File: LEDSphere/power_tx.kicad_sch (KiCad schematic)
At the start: 87 parts, among them J1 USB_C_Receptacle_USB2.0, M1 Motor_DC, Q1 BSS138, Q2 BSS138, Q3 BSS138, Q4 BSS138, Q5 BSS138, Q6 BSS138, Q7 Si2319CDS, Q8 Si2319CDS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

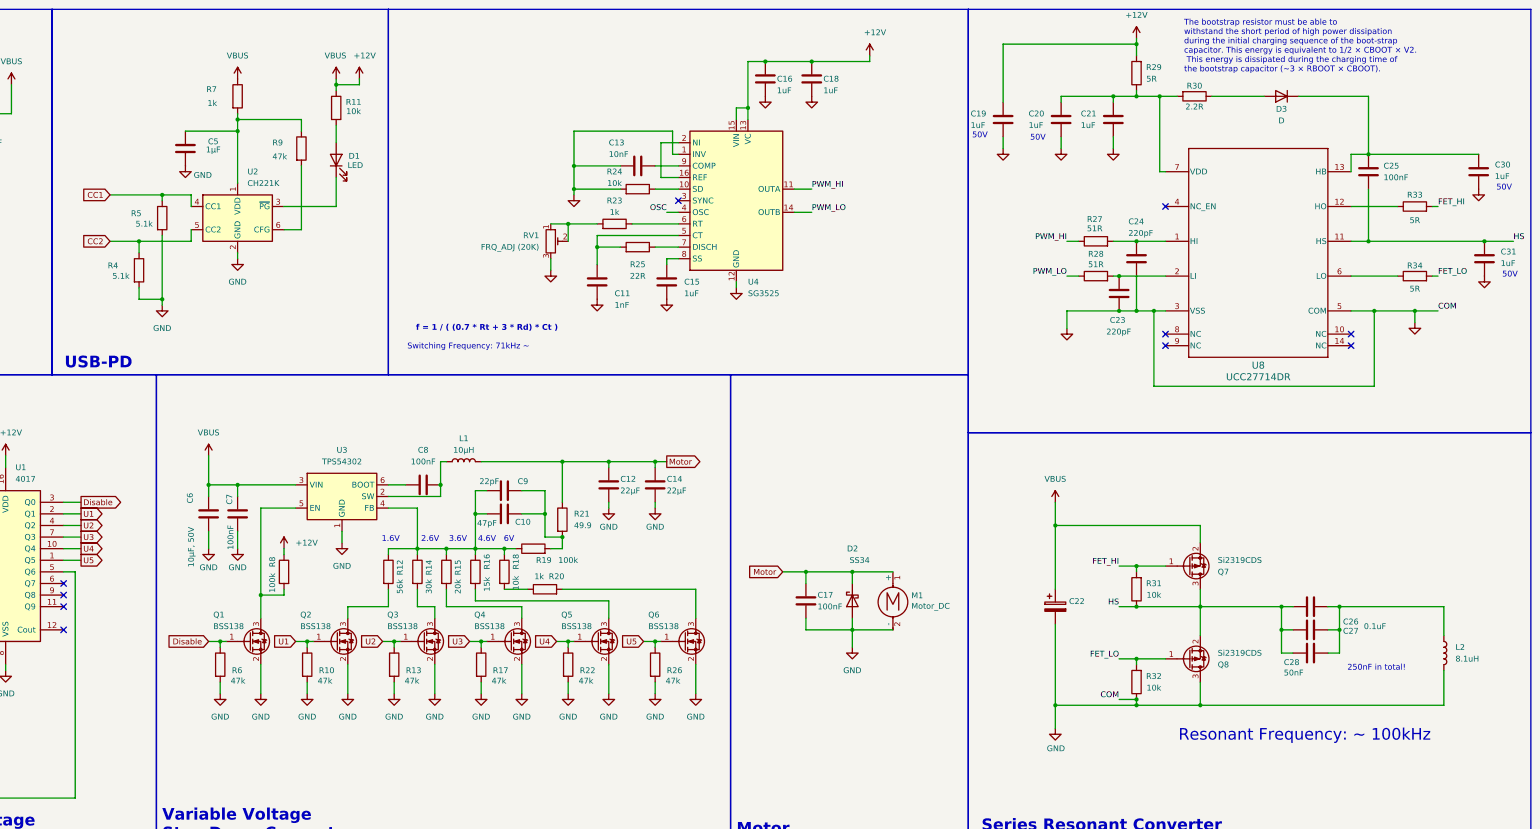
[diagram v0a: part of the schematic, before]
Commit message: Excluded Ground Pour
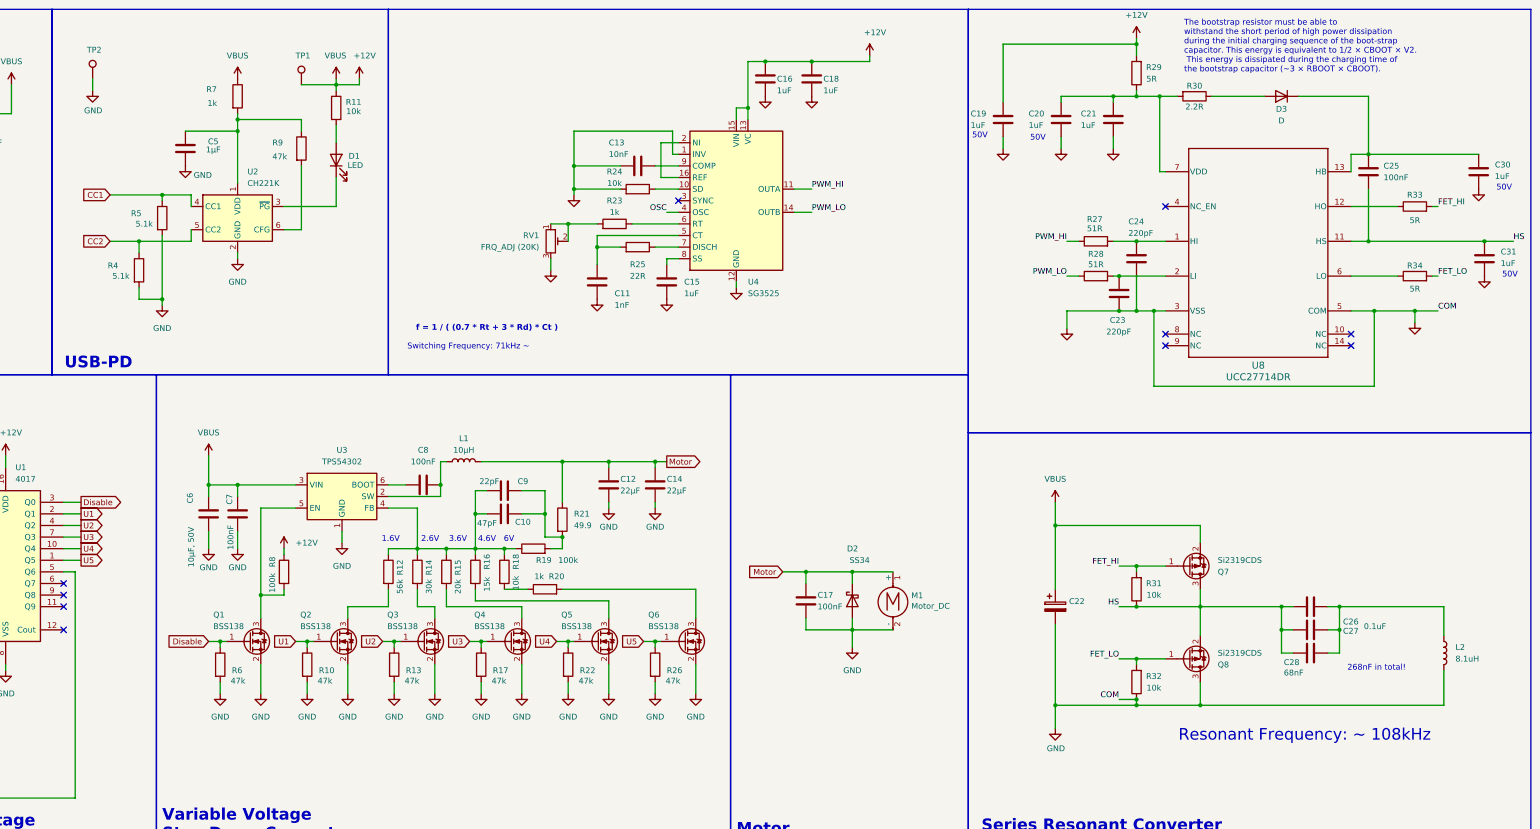
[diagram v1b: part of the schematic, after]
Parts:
- added TP1: TestPoint, TestPoint:TestPoint_Loop_D1.80mm_Drill1.0mm_Beaded, symbol Connector:TestPoint
- added TP2: TestPoint, TestPoint:TestPoint_Pad_D1.0mm, symbol Connector:TestPoint
- C28: value 50nF -> 68nF
- U8: footprint Footprints:D0014A -> Footprints:SOIC127P600X175-14N
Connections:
- net +12V: now also TP1.1
- net GND: now also TP2.1
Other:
- note added: "268nF in total!"
- note added: "Resonant Frequency: ~ 108kHz"
- note removed: "250nF in total!"
- note removed: "Resonant Frequency: ~ 100kHz"

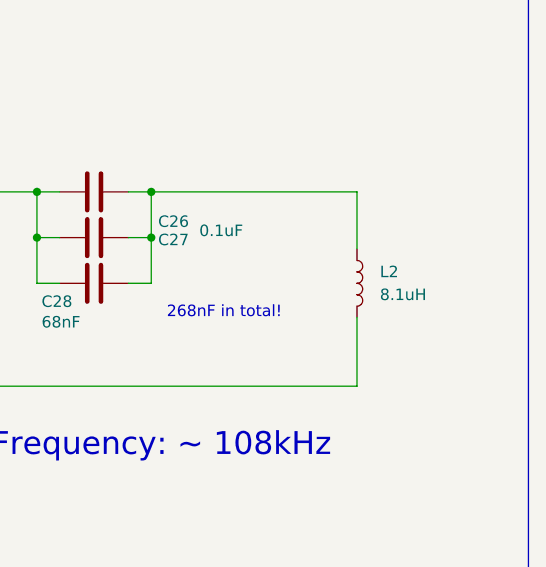
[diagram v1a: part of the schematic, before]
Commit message: Modify RX Schm. + Adjusted TX Coil
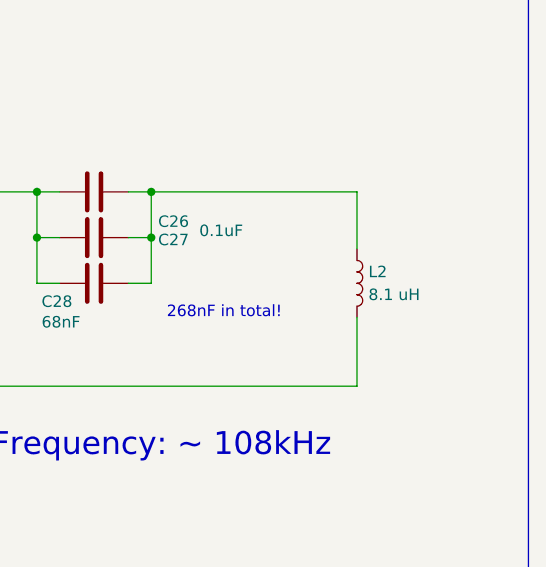
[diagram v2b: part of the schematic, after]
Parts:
- L2: value 8.1uH -> 8.1 uH
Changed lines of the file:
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@@
-	)
-	(symbol
-		(lib_id "Device:L")
-		(at 388.62 153.67 0)
-		(unit 1)
-		(body_style 1)
-		(exclude_from_sim no)
-		(in_bom yes)
-		(on_board yes)
-		(in_pos_files yes)
-		(dnp no)
-		(property "Reference" "L2"
-			(at 391.16 152.3999 0)
-			(show_name no)
-			(do_not_autoplace no)
-			(effects
-				(font
-					(size 1.27 1.27)
-				)
-				(justify left)
-			)
-		)
-		(property "Value" "8.1uH"
-			(at 391.16 154.94 0)
-			(show_name no)
-			(do_not_autoplace no)
-			(effects
-				(font
-					(size 1.27 1.27)
-				)
-				(justify left)
-			)
-		)
-		(property "Footprint" "Footprints:power_coil"
-			(at 388.62 153.67 0)
-			(hide yes)
-			(show_name no)
-			(do_not_autoplace no)
-			(effects
-				(font
-					(size 1.27 1.27)
-				)
-			)
-		)
-		(property "Datasheet" ""
-			(at 388.62 153.67 0)
-			(hide yes)
-			(show_name no)
-			(do_not_autoplace no)
-			(effects
-				(font
-					(size 1.27 1.27)
-				)
-			)
-		)
-		(property "Description" "Inductor"
-			(at 388.62 153.67 0)
-			(hide yes)
-			(show_name no)
-			(do_not_autoplace no)
-			(effects
-				(font
-					(size 1.27 1.27)
-				)
-			)
-		)
-		(pin "2"
-		)
-		(pin "1"
-		)
-		(instances
-			(project "power_tx"
-				(path "/f4cb5b8b-e797-4af7-88e9-03d9cedfe909"
-					(reference "L2")
-					(unit 1)
-				)
-			)
-		)
 	)
 	(symbol
@@
 					(unit 1)
 				)
+			)
+		)
+	)
+	(symbol
+		(lib_id "Device:L")
+		(at 388.62 153.67 0)
+		(unit 1)
+		(body_style 1)
+		(exclude_from_sim no)
+		(in_bom yes)
+		(on_board yes)
+		(in_pos_files yes)
+		(dnp no)
+		(fields_autoplaced yes)
+		(property "Reference" "L2"
+			(at 389.89 152.3999 0)
+			(show_name no)
+			(do_not_autoplace no)
+			(effects
+				(font
+					(size 1.27 1.27)
+				)
+				(justify left)
+			)
+		)
+		(property "Value" "8.1 uH"
+			(at 389.89 154.9399 0)
+			(show_name no)
+			(do_not_autoplace no)
+			(effects
+				(font
+					(size 1.27 1.27)
+				)
+				(justify left)
+			)
+		)
+		(property "Footprint" "Footprints:power_coil"
+			(at 388.62 153.67 0)
+			(hide yes)
+			(show_name no)
+			(do_not_autoplace no)
+			(effects
+				(font
+					(size 1.27 1.27)
+				)
+			)
+		)
+		(property "Datasheet" ""
+			(at 388.62 153.67 0)
+			(hide yes)
+			(show_name no)
+			(do_not_autoplace no)
+			(effects
+				(font
+					(size 1.27 1.27)
+				)
+			)
+		)
+		(property "Description" "Inductor"
+			(at 388.62 153.67 0)
+			(hide yes)
+			(show_name no)
+			(do_not_autoplace no)
+			(effects
+				(font
+					(size 1.27 1.27)
+				)
+			)
+		)
+		(pin "1"
+		)
+		(pin "2"
+		)
+		(instances
+			(project "power_tx"
+				(path "/f4cb5b8b-e797-4af7-88e9-03d9cedfe909"
+					(reference "L2")
+					(unit 1)
+				)

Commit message: Most Recent TX Board Changes
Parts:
- added C29: 68nF, Capacitor_SMD:C_0603_1608Metric, symbol Device:C
- added TP3: TestPoint, TestPoint:TestPoint_Loop_D1.80mm_Drill1.0mm_Beaded, symbol Connector:TestPoint
- L2: value 8.1 uH -> 5.8 uH
- TP2: footprint TestPoint:TestPoint_Pad_D1.0mm -> TestPoint:TestPoint_Loop_D1.80mm_Drill1.0mm_Beaded
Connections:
- net HS: now also C29.1
- net OSC: now also TP3.1
- net at C26.2, C27.2, C28.2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: now also C29.2
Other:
- note added: "400nF in total!"
- note added: "Resonant Frequency: ~ 104kHz"
- note removed: "268nF in total!"
- note removed: "Resonant Frequency: ~ 108kHz"

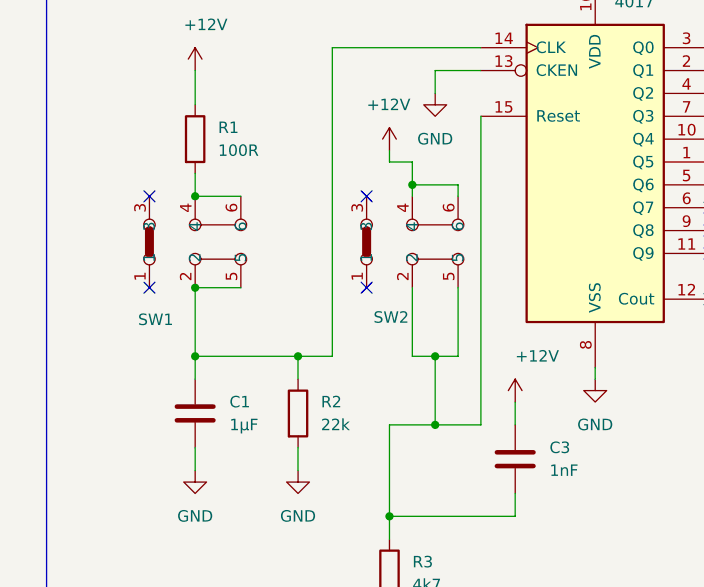
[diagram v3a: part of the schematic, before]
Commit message: Altered Button Part
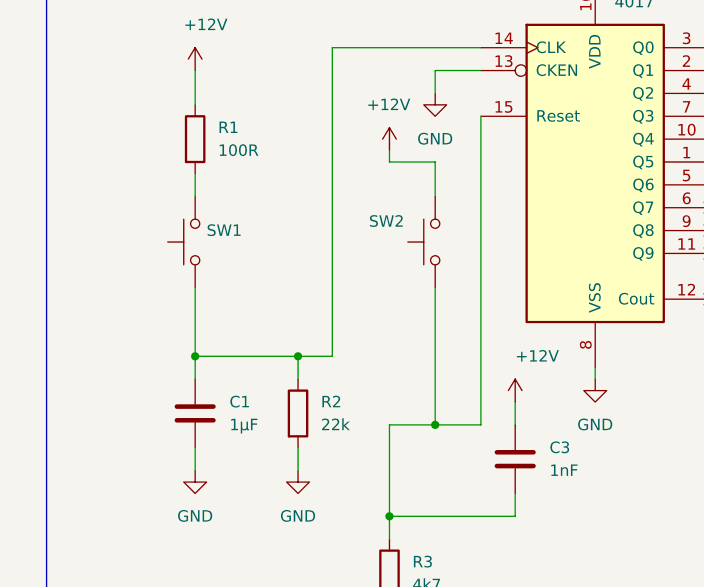
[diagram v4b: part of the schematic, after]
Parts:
- removed SW1, SW2: (no value), Footprints:XKB5858-X-F-75, symbol New_Library:XKB5858-X-F-75
- added SW1, SW2: SW_Push, Button_Switch_THT:SW_Tactile_SPST_Angled_PTS645Vx58-2LFS, symbol Switch:SW_Push
- D2: footprint Footprints:DIOM7959X262N -> Diode_SMD:D_SMA
- L1: footprint Inductor_SMD:L_Bourns_SRP7028A_7.3x6.6mm -> Inductor_SMD:L_Vishay_IHLP-3232; LCSC C5189958 -> (none)
- Q1: LCSC C7420339 -> (none)
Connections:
- net +12V: now also SW2.2
- net at C3.2, R3.1, U1.15 (Reset): now also SW2.1
- net at R1.2: now also SW1.2
- net at C1.1, R2.1, U1.14 (CLK): now also SW1.1
- no-connect marks 17 -> 13

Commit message: Edit 22uF Footprint to 1210
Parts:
- C12, C14: footprint Capacitor_SMD:C_0805_2012Metric -> Capacitor_SMD:C_1210_3225Metric
- D1: LCSC C84256 -> LSM0805412V
- SW1, SW2: Part # (none) -> PTS645VK58-2 LFS
- U1: LCSC C22390236 -> (none); Part # (none) -> CD4017BM96
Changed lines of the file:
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@@
 			)
 		)
-		(property "LCSC" "C84256"
+		(property "LCSC" "LSM0805412V"
 			(at 146.05 45.72 0)
 			(hide yes)
@@
 			)
 		)
-		(property "Datasheet" ""
+		(property "Datasheet" "https://www.digikey.com/en/products/detail/c-k/PTS645VK58-2-LFS/3861398"
 			(at 50.8 142.24 0)
 			(hide yes)
@@
 			)
 		)
+		(property "Part #" "PTS645VK58-2 LFS"
+			(at 55.88 142.24 90)
+			(hide yes)
+			(show_name no)
+			(do_not_autoplace no)
+			(effects
+				(font
+					(size 1.27 1.27)
+				)
+			)
+		)
 		(pin "1"
 		)
@@
 			)
 		)
-		(property "Description" "Trim-potentiometer"
+		(property "Description" "3362P-1-203LF"
 			(at 193.04 63.5 0)
 			(hide yes)
@@
 			)
 		)
-		(property "Datasheet" ""
+		(property "Datasheet" "https://www.digikey.com/en/products/detail/c-k/PTS645VK58-2-LFS/3861398"
 			(at 24.13 142.24 0)
 			(hide yes)
@@
 			)
 		)
+		(property "Part #" "PTS645VK58-2 LFS"
+			(at 29.21 142.24 90)
+			(hide yes)
+			(show_name no)
+			(do_not_autoplace no)
+			(effects
+				(font
+					(size 1.27 1.27)
+				)
+			)
+		)
 		(pin "1"
 		)
@@
 			)
 		)
-		(property "Footprint" "Capacitor_SMD:C_0805_2012Metric"
+		(property "Footprint" "Capacitor_SMD:C_1210_3225Metric"
 			(at 216.8652 120.65 0)
 			(hide yes)
@@
 			)
 		)
-		(property "LCSC" "C22390236"
+		(property "Part #" "CD4017BM96"
 			(at 73.66 133.35 0)
 			(hide yes)
@@
 			)
 		)
-		(property "Footprint" "Capacitor_SMD:C_0805_2012Metric"
+		(property "Footprint" "Capacitor_SMD:C_1210_3225Metric"
 			(at 206.7052 120.65 0)
 			(hide yes)

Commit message: Most up to date TX
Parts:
- added TP4, TP5: TestPoint, TestPoint:TestPoint_Pad_1.0x1.0mm, symbol Connector:TestPoint
- TP1, TP2, TP3: footprint TestPoint:TestPoint_Loop_D1.80mm_Drill1.0mm_Beaded -> TestPoint:TestPoint_THTPad_D2.0mm_Drill1.0mm
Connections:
- net GND: now also TP5.1
- net at C26.2, C27.2, C28.2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: now also TP4.1
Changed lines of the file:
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@@
 	)
 	(junction
+		(at 388.62 143.51)
+		(diameter 0)
+		(color 0 0 0 0)
+	)
+	(junction
 		(at 321.31 20.32)
 		(diameter 0)
@@
 	)
 	(junction
+		(at 388.62 165.1)
+		(diameter 0)
+		(color 0 0 0 0)
+	)
+	(junction
 		(at 120.65 151.13)
 		(diameter 0)
@@
 	(wire
 		(pts
+			(xy 388.62 165.1) (xy 394.97 165.1)
+		)
+		(stroke
+			(width 0)
+			(type default)
+		)
+	)
+	(wire
+		(pts
 			(xy 134.62 139.7) (xy 134.62 140.97)
 		)
@@
 	(wire
 		(pts
+			(xy 388.62 143.51) (xy 393.7 143.51)
+		)
+		(stroke
+			(width 0)
+			(type default)
+		)
+	)
+	(wire
+		(pts
 			(xy 167.64 143.51) (xy 167.64 146.05)
 		)
@@
 			)
 		)
-		(property "Footprint" "TestPoint:TestPoint_Loop_D1.80mm_Drill1.0mm_Beaded"
+		(property "Footprint" "TestPoint:TestPoint_THTPad_D2.0mm_Drill1.0mm"
 			(at 97.79 27.94 0)
 			(hide yes)
@@
 	)
 	(symbol
+		(lib_id "Connector:TestPoint")
+		(at 394.97 165.1 0)
+		(unit 1)
+		(body_style 1)
+		(exclude_from_sim no)
+		(in_bom yes)
+		(on_board yes)
+		(in_pos_files yes)
+		(dnp no)
+		(fields_autoplaced yes)
+		(property "Reference" "TP5"
+			(at 397.51 160.5279 0)
+			(show_name no)
+			(do_not_autoplace no)
+			(effects
+				(font
+					(size 1.27 1.27)
+				)
+				(justify left)
+			)
+		)
+		(property "Value" "TestPoint"
+			(at 397.51 163.0679 0)
+			(show_name no)
+			(do_not_autoplace no)
+			(effects
+				(font
+					(size 1.27 1.27)
+				)
+				(justify left)
+			)
+		)
+		(property "Footprint" "TestPoint:TestPoint_Pad_1.0x1.0mm"
+			(at 400.05 165.1 0)
+			(hide yes)
+			(show_name no)
+			(do_not_autoplace no)
+			(effects
+				(font
+					(size 1.27 1.27)
+				)
+			)
+		)
+		(property "Datasheet" ""
+			(at 400.05 165.1 0)
+			(hide yes)
+			(show_name no)
+			(do_not_autoplace no)
+			(effects
+				(font
+					(size 1.27 1.27)
+				)
+			)
+		)
+		(property "Description" "test point"
+			(at 394.97 165.1 0)
+			(hide yes)
+			(show_name no)
+			(do_not_autoplace no)
+			(effects
+				(font
+					(size 1.27 1.27)
+				)
+			)
+		)
+		(pin "1"
+		)
+		(instances
+			(project "power_tx"
+				(path "/f4cb5b8b-e797-4af7-88e9-03d9cedfe909"
+					(reference "TP5")
+					(unit 1)
+				)
+			)
+		)
+	)
+	(symbol
 		(lib_id "Device:R")
 		(at 382.27 55.88 90)
@@
 			)
 		)
-		(property "Footprint" "TestPoint:TestPoint_Loop_D1.80mm_Drill1.0mm_Beaded"
+		(property "Footprint" "TestPoint:TestPoint_THTPad_D2.0mm_Drill1.0mm"
 			(at 143.51 29.21 0)
 			(hide yes)
@@
 	)
 	(symbol
+		(lib_id "Connector:TestPoint")
+		(at 393.7 143.51 0)
+		(unit 1)
+		(body_style 1)
+		(exclude_from_sim no)
+		(in_bom yes)
+		(on_board yes)
+		(in_pos_files yes)
+		(dnp no)
+		(fields_autoplaced yes)
+		(property "Reference" "TP4"
+			(at 396.24 138.9379 0)
+			(show_name no)
+			(do_not_autoplace no)
+			(effects
+				(font
+					(size 1.27 1.27)
+				)
+				(justify left)
+			)
+		)
+		(property "Value" "TestPoint"
+			(at 396.24 141.4779 0)
+			(show_name no)
+			(do_not_autoplace no)
+			(effects
+				(font
+					(size 1.27 1.27)
+				)
+				(justify left)
+			)
+		)
+		(property "Footprint" "TestPoint:TestPoint_Pad_1.0x1.0mm"
+			(at 398.78 143.51 0)
+			(hide yes)
+			(show_name no)
+			(do_not_autoplace no)
+			(effects
+				(font
+					(size 1.27 1.27)
+				)
+			)
+		)
+		(property "Datasheet" ""
+			(at 398.78 143.51 0)
+			(hide yes)
+			(show_name no)
+			(do_not_autoplace no)
+			(effects
+				(font
+					(size 1.27 1.27)
+				)
+			)
+		)
+		(property "Description" "test point"
+			(at 393.7 143.51 0)
+			(hide yes)
+			(show_name no)
+			(do_not_autoplace no)
+			(effects
+				(font
+					(size 1.27 1.27)
+				)
+			)
+		)
+		(pin "1"
+		)
+		(instances
+			(project "power_tx"
+				(path "/f4cb5b8b-e797-4af7-88e9-03d9cedfe909"
+					(reference "TP4")
+					(unit 1)
+				)
+			)
+		)
+	)
+	(symbol
 		(lib_id "Transistor_FET:BSS138")
 		(at 127 151.13 0)
@@
 			)
 		)
-		(property "Footprint" "TestPoint:TestPoint_Loop_D1.80mm_Drill1.0mm_Beaded"
+		(property "Footprint" "TestPoint:TestPoint_THTPad_D2.0mm_Drill1.0mm"
 			(at 172.72 46.99 0)
 			(hide yes)
